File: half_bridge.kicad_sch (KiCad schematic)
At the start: 31 parts, among them Q1 IGC019S06S1XTMA1, Q2 IGC019S06S1XTMA1, U19 NCS2220AMUT1G, U4 ACS37030LLZATR-065B3, U5 LMG1205YFXR

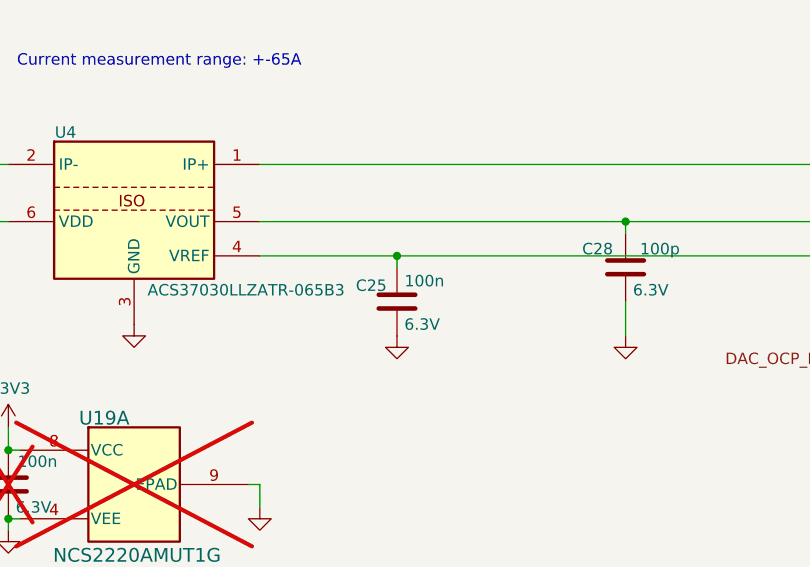
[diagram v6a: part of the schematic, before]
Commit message: changed the VREF capacitance (ACS37030) to 100pF
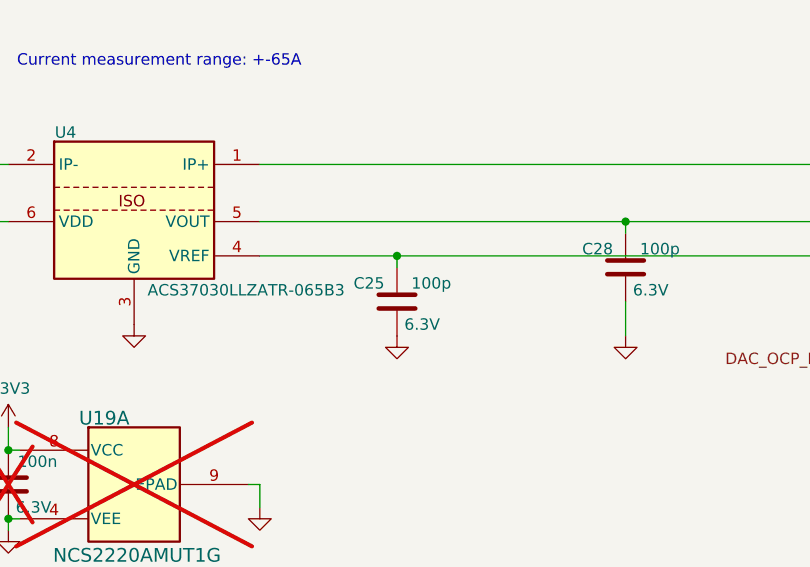
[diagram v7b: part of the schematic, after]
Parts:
- C25: Capacitance 100n -> 100p
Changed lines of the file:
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@@
-	)
-	(symbol
-		(lib_id "Device:C")
-		(at 160.02 109.22 0)
-		(unit 1)
-		(exclude_from_sim no)
-		(in_bom yes)
-		(on_board yes)
-		(dnp no)
-		(property "Reference" "C25"
-			(at 155.448 107.442 0)
-			(effects
-				(font
-					(size 1.27 1.27)
-				)
-				(justify left)
-			)
-		)
-		(property "Value" "~"
-			(at 161.036 106.68 0)
-			(effects
-				(font
-					(size 1.27 1.27)
-				)
-				(justify left)
-				(hide yes)
-			)
-		)
-		(property "Footprint" "Capacitor_SMD:C_0603_1608Metric_Pad1.08x0.95mm_HandSolder"
-			(at 160.9852 113.03 0)
-			(effects
-				(font
-					(size 1.27 1.27)
-				)
-				(hide yes)
-			)
-		)
-		(property "Datasheet" "~"
-			(at 160.02 109.22 0)
-			(effects
-				(font
-					(size 1.27 1.27)
-				)
-				(hide yes)
-			)
-		)
-		(property "Description" "100nF 6.3V X7R ±10% 0603 Multilayer Ceramic Capacitors MLCC - SMD/SMT ROHS"
-			(at 160.02 109.22 0)
-			(effects
-				(font
-					(size 1.27 1.27)
-				)
-				(hide yes)
-			)
-		)
-		(property "Capacitance" "100n"
-			(at 163.068 106.934 0)
-			(effects
-				(font
-					(size 1.27 1.27)
-				)
-			)
-		)
-		(property "Voltage Rating" "6.3V"
-			(at 162.814 111.76 0)
-			(effects
-				(font
-					(size 1.27 1.27)
-				)
-			)
-		)
-		(pin "1"
-		)
-		(pin "2"
-		)
-		(instances
-			(project "NanoGaN"
-				(path "/aa8a494f-605e-4a00-9d3c-daec94709fcb/47075a52-6063-4b82-8884-2b908f359801"
-					(reference "C26")
-					(unit 1)
-				)
-				(path "/aa8a494f-605e-4a00-9d3c-daec94709fcb/6f3a55d2-28c8-407e-8c9d-28f4ee320cbb"
-					(reference "C25")
-					(unit 1)
-				)
-				(path "/aa8a494f-605e-4a00-9d3c-daec94709fcb/e0a1170f-dabd-4224-bbe3-5bcec1b89854"
-					(reference "C33")
-					(unit 1)
-				)
-			)
-		)
 	)
 	(symbol
@@
 					(unit 1)
 				)
+			)
+		)
+	)
+	(symbol
+		(lib_id "Device:C")
+		(at 160.02 109.22 0)
+		(unit 1)
+		(exclude_from_sim no)
+		(in_bom yes)
+		(on_board yes)
+		(dnp no)
+		(property "Reference" "C25"
+			(at 155.194 107.188 0)
+			(effects
+				(font
+					(size 1.27 1.27)
+				)
+				(justify left)
+			)
+		)
+		(property "Value" "~"
+			(at 161.036 106.68 0)
+			(effects
+				(font
+					(size 1.27 1.27)
+				)
+				(justify left)
+				(hide yes)
+			)
+		)
+		(property "Footprint" "Capacitor_SMD:C_0603_1608Metric_Pad1.08x0.95mm_HandSolder"
+			(at 160.9852 113.03 0)
+			(effects
+				(font
+					(size 1.27 1.27)
+				)
+				(hide yes)
+			)
+		)
+		(property "Datasheet" "~"
+			(at 160.02 109.22 0)
+			(effects
+				(font
+					(size 1.27 1.27)
+				)
+				(hide yes)
+			)
+		)
+		(property "Description" "100pF 50V C0G ±5% 0603 Multilayer Ceramic Capacitors MLCC - SMD/SMT ROHS"
+			(at 160.02 109.22 0)
+			(effects
+				(font
+					(size 1.27 1.27)
+				)
+				(hide yes)
+			)
+		)
+		(property "Voltage Rating" "6.3V"
+			(at 162.814 111.76 0)
+			(effects
+				(font
+					(size 1.27 1.27)
+				)
+			)
+		)
+		(property "Capacitance" "100p"
+			(at 163.83 107.188 0)
+			(effects
+				(font
+					(size 1.27 1.27)
+				)
+			)
+		)
+		(pin "1"
+		)
+		(pin "2"
+		)
+		(instances
+			(project "NanoGaN"
+				(path "/aa8a494f-605e-4a00-9d3c-daec94709fcb/47075a52-6063-4b82-8884-2b908f359801"
+					(reference "C26")
+					(unit 1)
+				)
+				(path "/aa8a494f-605e-4a00-9d3c-daec94709fcb/6f3a55d2-28c8-407e-8c9d-28f4ee320cbb"
+					(reference "C25")
+					(unit 1)
+				)
+				(path "/aa8a494f-605e-4a00-9d3c-daec94709fcb/e0a1170f-dabd-4224-bbe3-5bcec1b89854"
+					(reference "C33")
+					(unit 1)
+				)

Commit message: schematic and PCB reviews are done, ready for release and first order.
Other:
- note added: "Due to layout reasons, the current measurement has to be inverted in the software."
- note removed: "Add more capacitors close to semiconductor switches if there is enough space"
- note removed: "to be later adjusted"
- company: (none) -> Eren Akbayin
- title: (none) -> NanoGaN
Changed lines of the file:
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@@
 	(generator_version "9.0")
 	(paper "A4")
+	(title_block
+		(title "NanoGaN")
+		(date "2026-02-22")
+		(rev "A01")
+		(company "Eren Akbayin")
+	)
 	(rectangle
 		(start 12.7 139.7)
@@
 		)
 	)
-	(text "to be later adjusted"
+	(text "Due to layout reasons, the current measurement has to be inverted in the software."
 		(exclude_from_sim no)
-		(at 74.422 188.976 0)
+		(at 149.86 87.63 0)
 		(effects
 			(font
@@
 		)
 	)
-	(text "Add more capacitors close \nto semiconductor switches\nif there is enough space"
-		(exclude_from_sim no)
-		(at 29.464 107.696 0)
-		(effects
-			(font
-				(size 1.27 1.27)
-			)
-		)
-	)
 	(text "V_Hysteresis = (3.3V x 10kohm) / ( 39kohm + 10kohm) = 0.67V"
 		(exclude_from_sim no)
@@
 	(text "Current measurement range: +-65A"
 		(exclude_from_sim no)
-		(at 133.604 82.55 0)
+		(at 125.984 85.344 0)
 		(effects
 			(font
